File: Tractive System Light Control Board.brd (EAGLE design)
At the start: 88.9 x 51.1 mm, 63 parts, among them J1 MOLEX_CLICKMATE-2-VERTICAL, J2 MOLEX_CLICKMATE-2-VERTICAL, J3 MOLEX_CLICKMATE-2-VERTICAL, J4 MOLEX_CLICKMATE-2-VERTICAL, T1 750313734, T3 LMC555, U1 ISO7221, U12 SN6501DBVR, U2 TPS562219, U3 SN74LVC1G00DRL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

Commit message: Small Layout Changes, about to start BOM
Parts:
- moved C11 0.90 mm to (74.9, 15.2), turned to 0 degrees
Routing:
- net +5V: track 36.3 -> 37.2 mm
- net N$12: vias 2 -> 4

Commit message: BOM Done, files next
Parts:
- removed C90, C91: 10uF, rcl:C1206
- added C12, C13: 10uF, rcl:C0805
- R32: value 47R -> 47
- renumbered R72 to R32, TP2 to TP1
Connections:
- net +5V/1: now also C13.1; no longer C91.1
- net GND1: now also C12.2, C13.2; no longer C90.2, C91.2
- net N$43: now also C12.1; no longer C90.1
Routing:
- net GND1: track 18.0 -> 17.2 mm

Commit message: BOM Done, about to generate files
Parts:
- moved R19 2.62 mm to (23.5, 37.5), turned to 270 degrees
- moved R22 1.42 mm to (23.5, 28.6), turned to 270 degrees
- moved R23 1.42 mm to (20.3, 24.8)
- moved R21 0.90 mm to (23.5, 33.0), turned to 270 degrees
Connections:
- removed net B-: J2.1, R23.2, R6.P$2
- net GND1: now also J2.1, R23.2, R6.P$2
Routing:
- net N$18: track 8.26 -> 2.92 mm
- net BATT_V_REFERENCE: track 15.9 -> 12.9 mm
- net GND1: vias 15 -> 20
- removed copper zone on layer 1, net B-

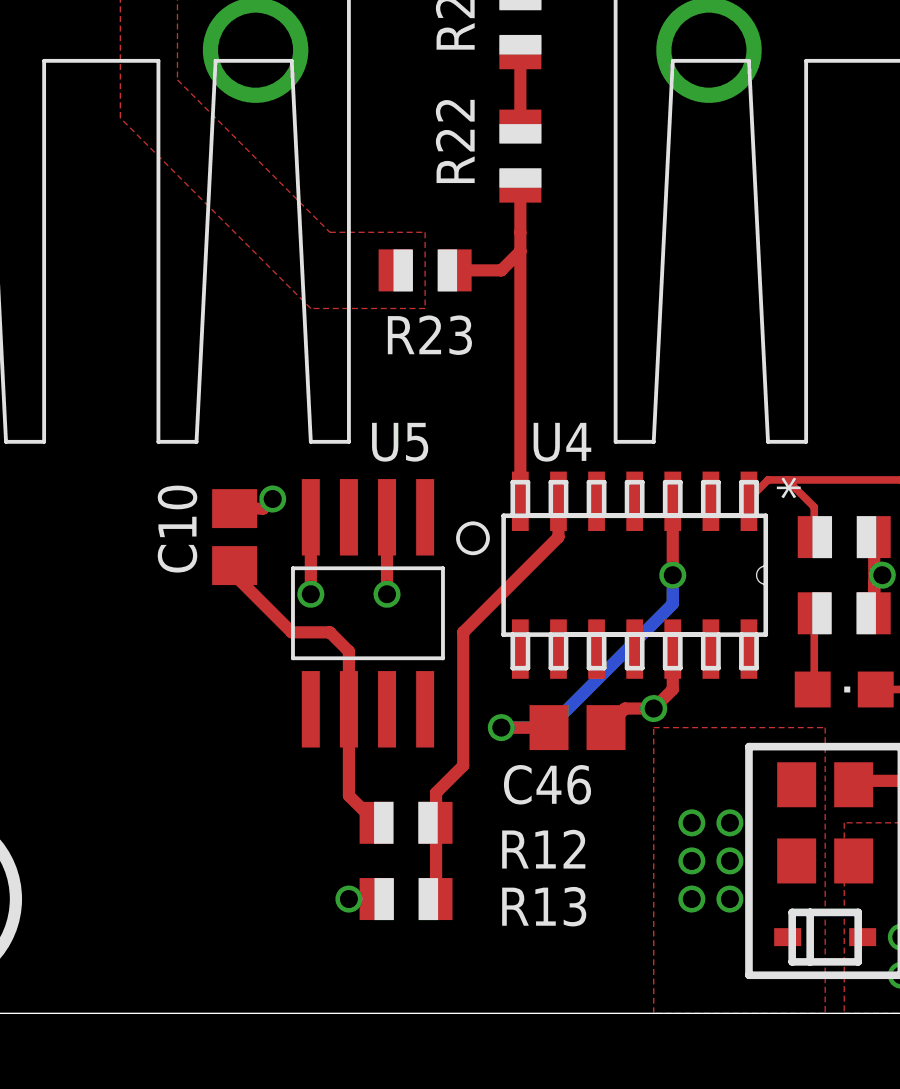
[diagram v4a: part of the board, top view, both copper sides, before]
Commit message: Fixed comparator and BOM, about to generate files
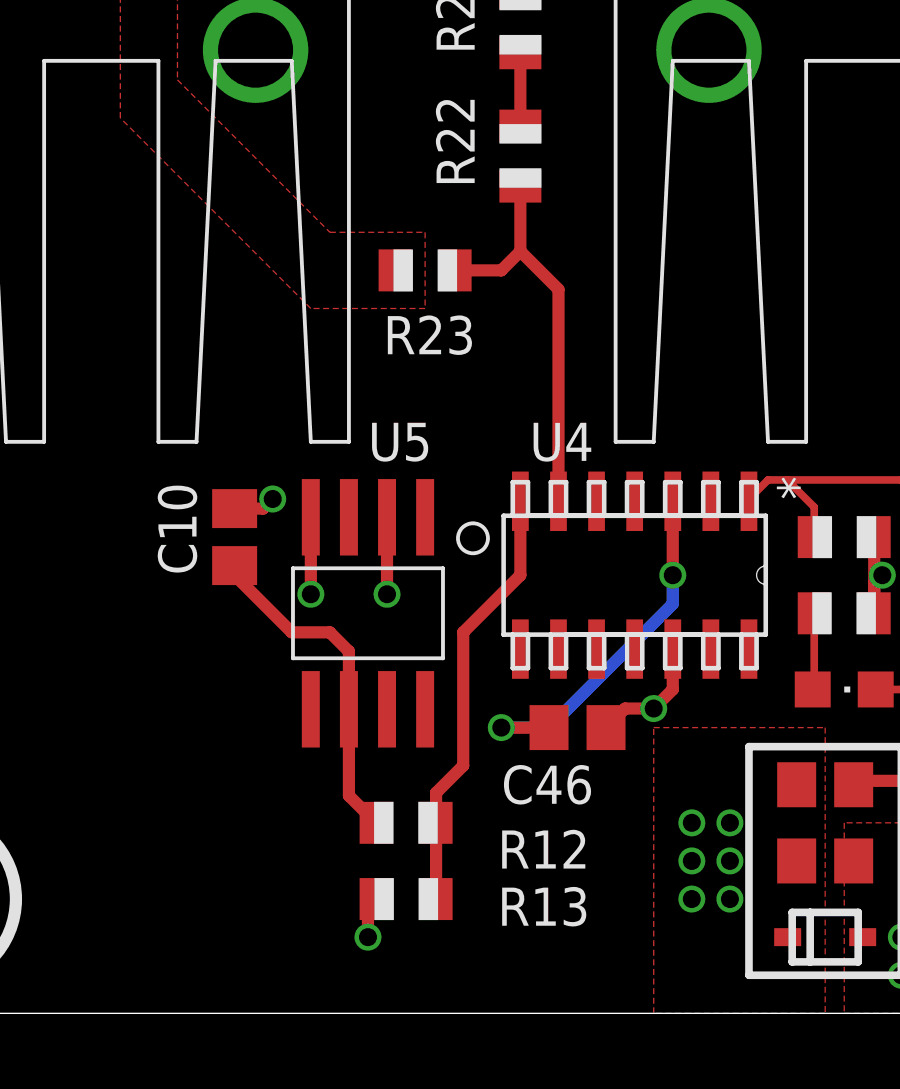
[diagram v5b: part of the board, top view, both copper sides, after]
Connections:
- net 0.9V_REF: now also U4.7; no longer U4.6
- net BATT_V_REFERENCE: now also U4.6; no longer U4.7
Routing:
- net BATT_V_REFERENCE: track 12.9 -> 13.5 mm
- net 0.9V_REF: track 14.9 -> 14.4 mm
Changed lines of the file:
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@@
 </element>
 <element name="R8" library="adafruit" package="R0805" value="20k" x="85.09" y="12.7" smashed="yes" rot="R90">
-<attribute name="PARTNO" value="ERJ-3EKF2002V" x="78.74" y="12.7" size="1.778" layer="27" rot="R90" display="off"/>
+<attribute name="PARTNO" value="ERA-6AEB204V" x="78.74" y="12.7" size="1.778" layer="27" rot="R90" display="off"/>
 <attribute name="NAME" x="85.979" y="15.113" size="1.27" layer="25" rot="R90"/>
 <attribute name="VALUE" x="87.376" y="11.938" size="1.27" layer="27" rot="R90"/>
 </element>
 <element name="R20" library="adafruit" package="R0805" value="10.5k" x="71.755" y="14.605" smashed="yes" rot="R270">
-<attribute name="PARTNO" value="ERA-8ARW1052V" x="66.675" y="14.605" size="1.778" layer="27" rot="R270" display="off"/>
+<attribute name="PARTNO" value="ERA-6AEB1052V" x="66.675" y="14.605" size="1.778" layer="27" rot="R270" display="off"/>
 <attribute name="NAME" x="72.644" y="17.018" size="1.27" layer="25" rot="R90"/>
 <attribute name="VALUE" x="69.469" y="15.367" size="1.27" layer="27" rot="R270"/>
@@
 <wire x1="14.92" y1="16.825" x2="15.24" y2="17.145" width="0.4064" layer="1"/>
 <via x="15.24" y="17.145" extent="1-16" drill="0.6"/>
-<wire x1="18.685" y1="3.81" x2="17.78" y2="3.81" width="0.4064" layer="1"/>
-<via x="17.78" y="3.81" extent="1-16" drill="0.6"/>
+<via x="18.415" y="2.54" extent="1-16" drill="0.6"/>
 <contactref element="C12" pad="2"/>
 <contactref element="C13" pad="2"/>
@@
 </polygon>
 <via x="44.45" y="32.385" extent="1-16" drill="0.6"/>
+<wire x1="18.415" y1="2.54" x2="18.415" y2="3.54" width="0.4064" layer="1"/>
+<wire x1="18.415" y1="3.54" x2="18.685" y2="3.81" width="0.4064" layer="1"/>
 </signal>
 <signal name="HV_INDICATOR_SIGNAL_HV">
@@
 <contactref element="R22" pad="2"/>
 <contactref element="R23" pad="1"/>
-<contactref element="U4" pad="7"/>
-<wire x1="23.495" y1="27.575" x2="23.495" y2="26.035" width="0.4064" layer="1"/>
-<wire x1="23.495" y1="26.035" x2="23.495" y2="25.4" width="0.4064" layer="1"/>
+<wire x1="23.495" y1="27.575" x2="23.495" y2="25.4" width="0.4064" layer="1"/>
 <wire x1="23.495" y1="25.4" x2="22.86" y2="24.765" width="0.4064" layer="1"/>
 <wire x1="22.86" y1="24.765" x2="21.32" y2="24.765" width="0.4064" layer="1"/>
-<wire x1="23.495" y1="17.0688" x2="23.495" y2="25.4" width="0.4064" layer="1"/>
+<contactref element="U4" pad="6"/>
+<wire x1="24.765" y1="17.0688" x2="24.765" y2="24.13" width="0.4064" layer="1"/>
+<wire x1="24.765" y1="24.13" x2="23.495" y2="25.4" width="0.4064" layer="1"/>
 </signal>
 <signal name="N$31">
@@
 </signal>
 <signal name="0.9V_REF">
-<contactref element="U4" pad="6"/>
 <contactref element="R12" pad="2"/>
 <contactref element="R13" pad="1"/>
@@
 <wire x1="20.685" y1="7.35" x2="21.59" y2="8.255" width="0.4064" layer="1"/>
 <wire x1="21.59" y1="8.255" x2="21.59" y2="12.7" width="0.4064" layer="1"/>
-<wire x1="21.59" y1="12.7" x2="24.765" y2="15.875" width="0.4064" layer="1"/>
-<wire x1="24.765" y1="15.875" x2="24.765" y2="17.0688" width="0.4064" layer="1"/>
+<contactref element="U4" pad="7"/>
+<wire x1="23.495" y1="17.0688" x2="23.495" y2="14.605" width="0.4064" layer="1"/>
+<wire x1="23.495" y1="14.605" x2="21.59" y2="12.7" width="0.4064" layer="1"/>
 </signal>
 <signal name="1.8V_REF">

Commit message: A few minor layout tweaks. Regenerated gerbers and BOM
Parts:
- R1, R6: value (none) -> 10k
- moved C5 2.62 mm to (79.4, 48.3), turned to 90 degrees
- moved R3 1.91 mm to (76.8, 48.3), turned to 270 degrees
- moved C11 1.27 mm to (74.9, 14.0)
- turned R2 to 90 degrees
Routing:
- net GND: track 30.2 -> 24.9 mm, vias 27 -> 25
- net SS_5V1: track 3.07 -> 4.97 mm
- net VFB_5V1: track 7.39 -> 5.83 mm
- net 555_TIMER_CONTROL: track 2.94 -> 3.63 mm
- net N$12: track 36.3 -> 35.6 mm, vias 4 -> 2
- net N$13: vias 2 -> 0
- net GND1: vias 20 -> 19
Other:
- board size 88.9 x 51.1 mm -> 88.9 x 50.8 mm
- board text added: "HIGH VOLTAGE"
- board text removed: "Tractive System"

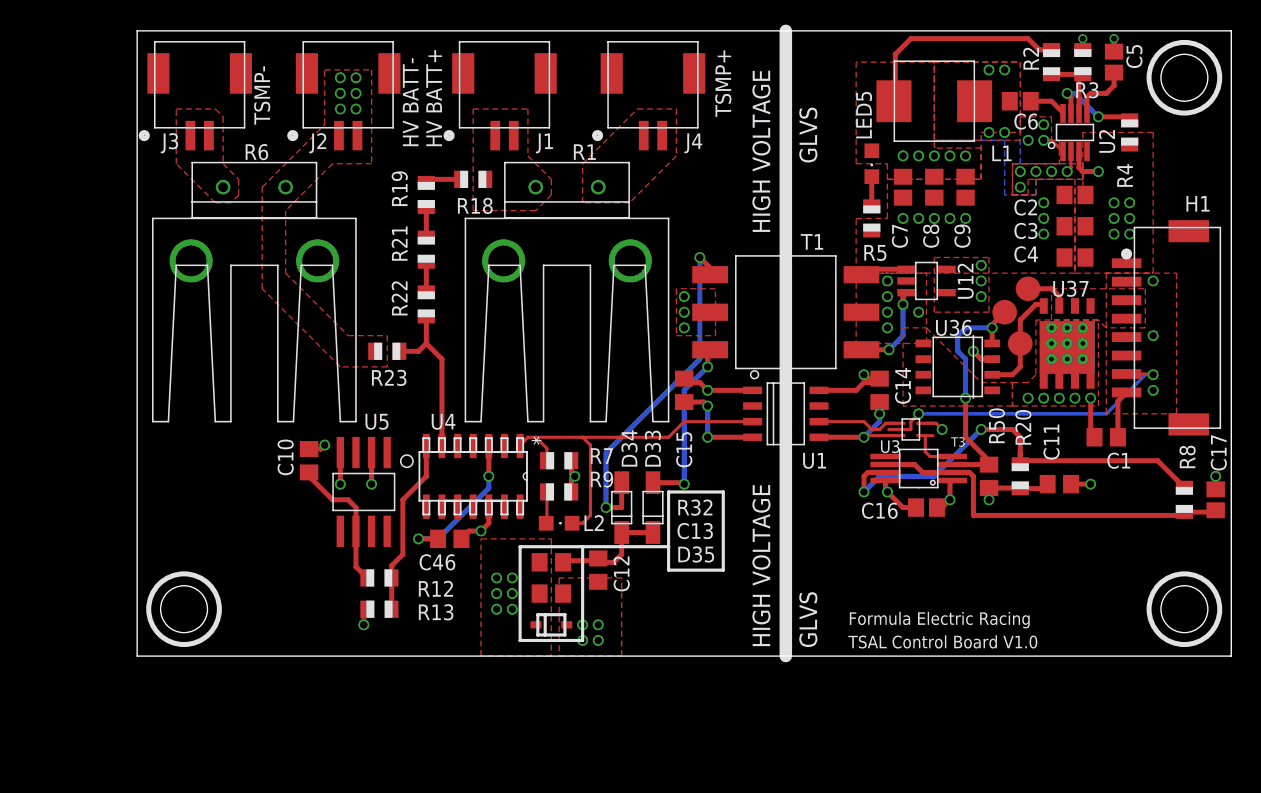
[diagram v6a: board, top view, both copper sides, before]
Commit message: Fixed 10k Resistors- TSAL Control Board V2.0- Ready To Order
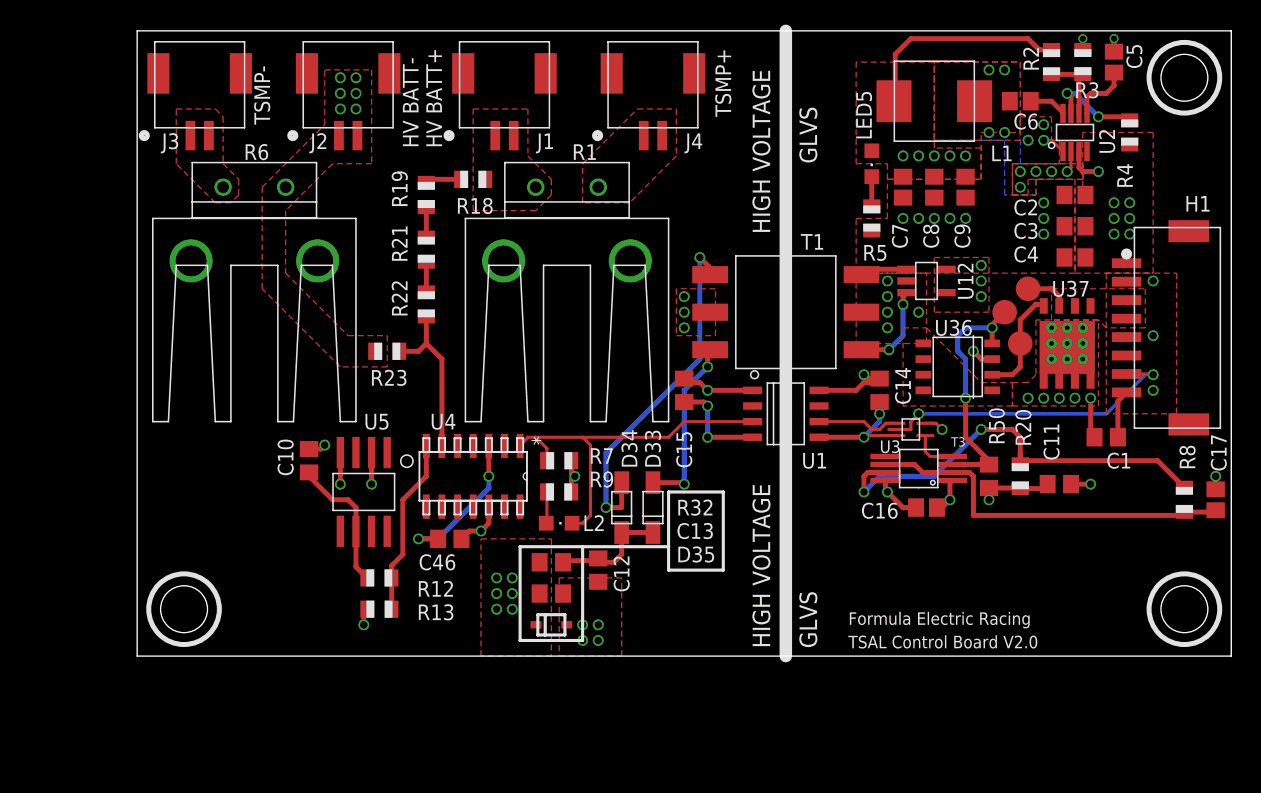
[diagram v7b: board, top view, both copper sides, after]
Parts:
- R1, R6: value 10k -> (none)
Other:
- board text added: "TSAL Control Board V2.0"
- board text removed: "TSAL Control Board V1.0"
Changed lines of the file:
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@@
 <?xml version="1.0" encoding="utf-8"?>
 <!DOCTYPE eagle SYSTEM "eagle.dtd">
-<eagle version="7.3.0">
+<eagle version="7.5.0">
 <drawing>
 <settings>
@@
 <wire x1="36.195" y1="8.89" x2="36.195" y2="1.27" width="0.254" layer="21"/>
 <wire x1="36.195" y1="1.27" x2="31.115" y2="1.27" width="0.254" layer="21"/>
-<text x="57.785" y="0.635" size="1.016" layer="21">TSAL Control Board V1.0</text>
+<text x="57.785" y="0.635" size="1.016" layer="21">TSAL Control Board V2.0</text>
 <text x="57.785" y="2.54" size="1.016" layer="21">Formula Electric Racing</text>
 <text x="51.435" y="0.635" size="1.4224" layer="21" rot="R90">HIGH VOLTAGE</text>
@@
 <attribute name="PARTNO" value="581002B02500G" x="34.925" y="38.1" size="1.778" layer="27" rot="R180" display="off"/>
 </element>
-<element name="R1" library="FormE" package="TO-220-2" value="10k" x="34.925" y="38.1" smashed="yes" rot="R180">
+<element name="R1" library="FormE" package="TO-220-2" value="" x="34.925" y="38.1" smashed="yes" rot="R180">
 <attribute name="NAME" x="35.33" y="40.315" size="1.27" layer="21"/>
 <attribute name="PARTNO" value="RTO020F10001JTE3" x="34.925" y="38.1" size="1.778" layer="27" rot="R180" display="off"/>
 </element>
-<element name="R6" library="FormE" package="TO-220-2" value="10k" x="9.525" y="38.1" smashed="yes" rot="R180">
+<element name="R6" library="FormE" package="TO-220-2" value="" x="9.525" y="38.1" smashed="yes" rot="R180">
 <attribute name="NAME" x="8.66" y="40.315" size="1.27" layer="21"/>
 <attribute name="PARTNO" value="RTO020F10001JTE3" x="9.525" y="38.1" size="1.778" layer="27" rot="R180" display="off"/>
